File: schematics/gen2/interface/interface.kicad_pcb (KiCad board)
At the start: 2 copper layers, 100 x 91 mm, 18 parts, among them U1 74LS00, U2 74LS00, U4 74LS245, U5 74LS193, U6 74LS193, U7 74LS193, U8 74LS193

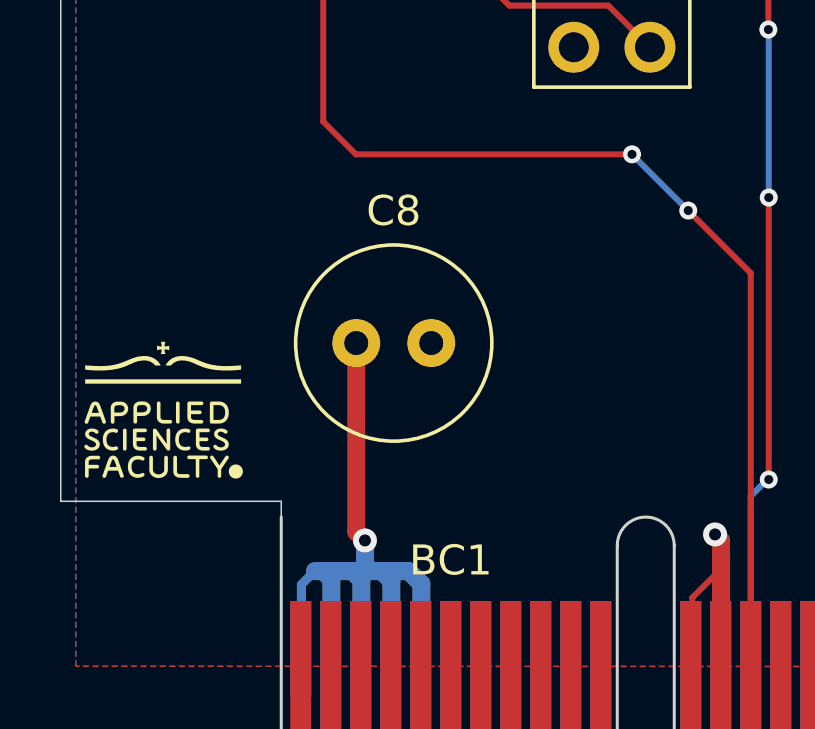
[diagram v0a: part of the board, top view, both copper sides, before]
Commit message: fix(kicad): vcc zones
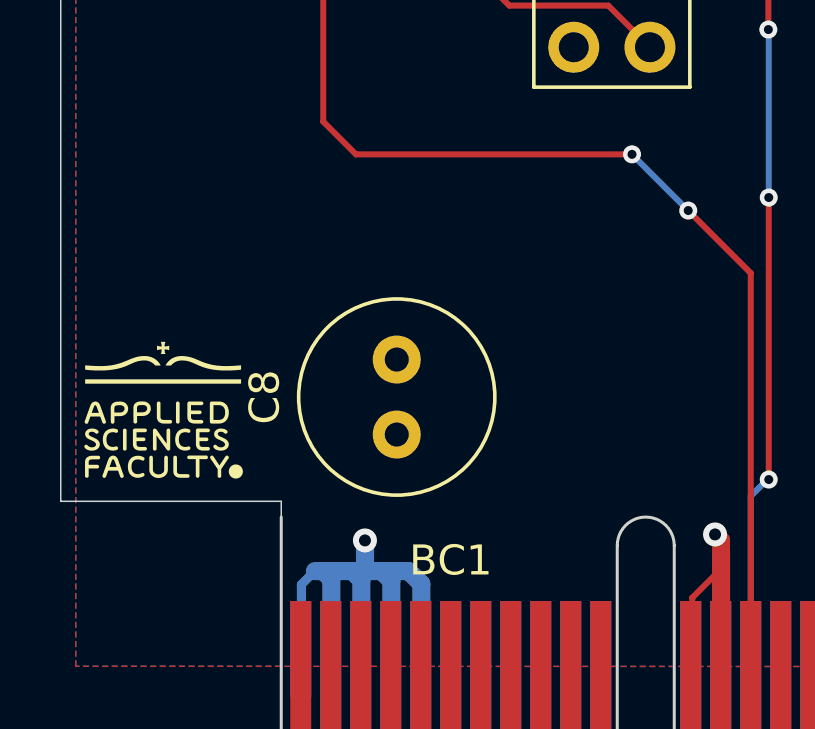
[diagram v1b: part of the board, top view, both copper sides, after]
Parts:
- moved C8 3.34 mm to (96.8, 110.9), turned to 90 degrees
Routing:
- net VCC: track 58.4 -> 51.7 mm
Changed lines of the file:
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@@
 			(pinfunction "VCC")
 			(pintype "power_in")
+			(zone_connect 0)
 		)
 		(embedded_fonts no)
@@
 			(pinfunction "VCC")
 			(pintype "power_in")
+			(zone_connect 0)
 		)
 		(embedded_fonts no)
@@
 			(pinfunction "VCC")
 			(pintype "power_in")
+			(zone_connect 0)
 		)
 		(embedded_fonts no)
@@
 			(pinfunction "VCC")
 			(pintype "power_in")
+			(zone_connect 0)
 		)
 		(embedded_fonts no)
@@
 			(pinfunction "VCC")
 			(pintype "power_in")
+			(zone_connect 0)
 		)
 		(embedded_fonts no)
@@
 	(footprint "Capacitor_THT:C_Radial_D6.3mm_H5.0mm_P2.50mm"
 		(layer "F.Cu")
-		(at 95.5 107.85)
+		(at 96.85 110.9 90)
 		(descr "C, Radial series, Radial, pin pitch=2.50mm, diameter=6.3mm, height=5mm, Non-Polar Electrolytic Capacitor")
 		(tags "C Radial series Radial pin pitch 2.50mm diameter 6.3mm height 5mm Non-Polar Electrolytic Capacitor")
 		(property "Reference" "C8"
-			(at 1.25 -4.4 0)
+			(at 1.25 -4.4 90)
 			(layer "F.SilkS")
 			(effects
@@
 		)
 		(property "Value" "C"
-			(at 1.25 4.4 0)
+			(at 1.25 4.4 90)
 			(layer "F.Fab")
 			(effects
@@
 		)
 		(property "Datasheet" "~"
-			(at 0 0 0)
+			(at 0 0 90)
 			(layer "F.Fab")
 			(hide yes)
@@
 		)
 		(property "Description" "Unpolarized capacitor"
-			(at 0 0 0)
+			(at 0 0 90)
 			(layer "F.Fab")
 			(hide yes)
@@
 		)
 		(fp_text user "${REFERENCE}"
-			(at 1.25 0 0)
+			(at 1.25 0 90)
 			(layer "F.Fab")
 			(effects
@@
 		)
 		(pad "1" thru_hole circle
-			(at 0 0)
+			(at 0 0 90)
 			(size 1.6 1.6)
 			(drill 0.8)
@@
 		)
 		(pad "2" thru_hole circle
-			(at 2.5 0)
+			(at 2.5 0 90)
 			(size 1.6 1.6)
 			(drill 0.8)
@@
 			(pinfunction "VCC")
 			(pintype "power_in")
+			(zone_connect 0)
 		)
 		(embedded_fonts no)
@@
 	)
 	(segment
-		(start 95.5 114.14)
-		(end 95.5 107.85)
-		(width 0.6)
-		(layer "F.Cu")
-		(net 6)
-	)
-	(segment
 		(start 113.085 36.04)
 		(end 112.79 36.04)
@@
 		(width 0.6)
 		(layer "F.Cu")
-		(net 6)
-	)
-	(segment
-		(start 95.79 114.43)
-		(end 95.5 114.14)
-		(width 0.6)
-		(layer "F.Cu")
